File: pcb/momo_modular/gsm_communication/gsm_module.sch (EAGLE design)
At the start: 22 parts, among them U1 PIC16LF1823, U2 TI-HIGHSIDE-PFET, U3 SIM900, U4 ESD-SMF05C

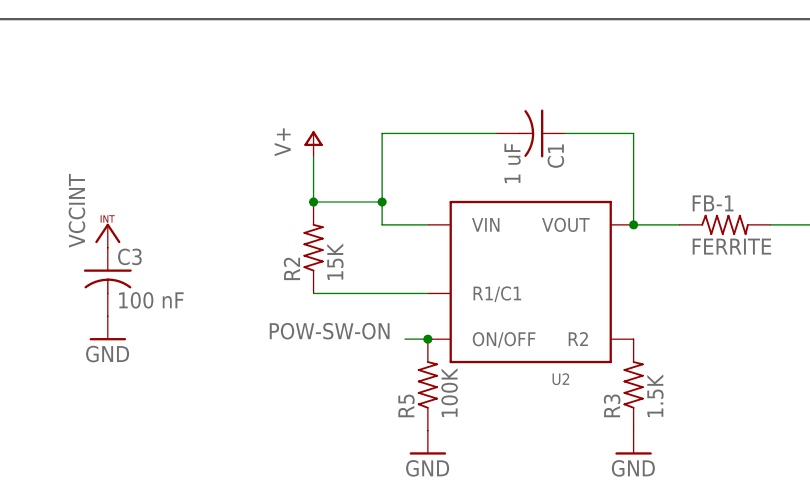
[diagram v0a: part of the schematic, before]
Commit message: Fixed C1 wiring to properly do soft-start
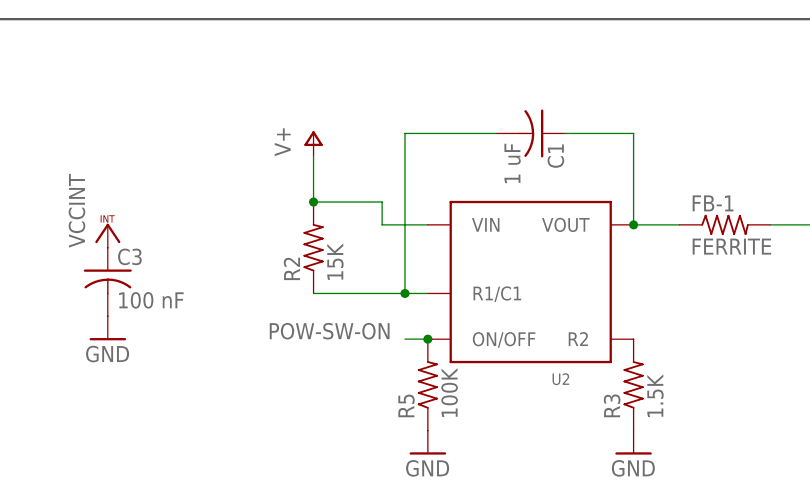
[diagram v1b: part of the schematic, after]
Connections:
- net N$3: now also C1.2
- net V+: no longer C1.2
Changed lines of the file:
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@@
 <?xml version="1.0" encoding="utf-8"?>
 <!DOCTYPE eagle SYSTEM "eagle.dtd">
-<eagle version="6.4">
+<eagle version="6.5.0">
 <drawing>
 <settings>
@@
 <wire x1="78.74" y1="93.98" x2="71.12" y2="93.98" width="0.1524" layer="91"/>
 <junction x="71.12" y="93.98"/>
-<pinref part="C1" gate="G$1" pin="2"/>
-<wire x1="91.44" y1="101.6" x2="78.74" y2="101.6" width="0.1524" layer="91"/>
-<wire x1="78.74" y1="101.6" x2="78.74" y2="93.98" width="0.1524" layer="91"/>
-<junction x="78.74" y="93.98"/>
 <pinref part="U2" gate="G$1" pin="VIN"/>
 </segment>
@@
 <segment>
 <pinref part="R2" gate="G$1" pin="1"/>
-<wire x1="71.12" y1="83.82" x2="83.82" y2="83.82" width="0.1524" layer="91"/>
+<wire x1="71.12" y1="83.82" x2="81.28" y2="83.82" width="0.1524" layer="91"/>
 <pinref part="U2" gate="G$1" pin="R1/C1"/>
-</segment>
-</net>
+<pinref part="C1" gate="G$1" pin="2"/>
+<wire x1="81.28" y1="83.82" x2="83.82" y2="83.82" width="0.1524" layer="91"/>
+<wire x1="91.44" y1="101.6" x2="81.28" y2="101.6" width="0.1524" layer="91"/>
+<wire x1="81.28" y1="101.6" x2="81.28" y2="83.82" width="0.1524" layer="91"/>
+<junction x="81.28" y="83.82"/>
+</segment>
+</net>

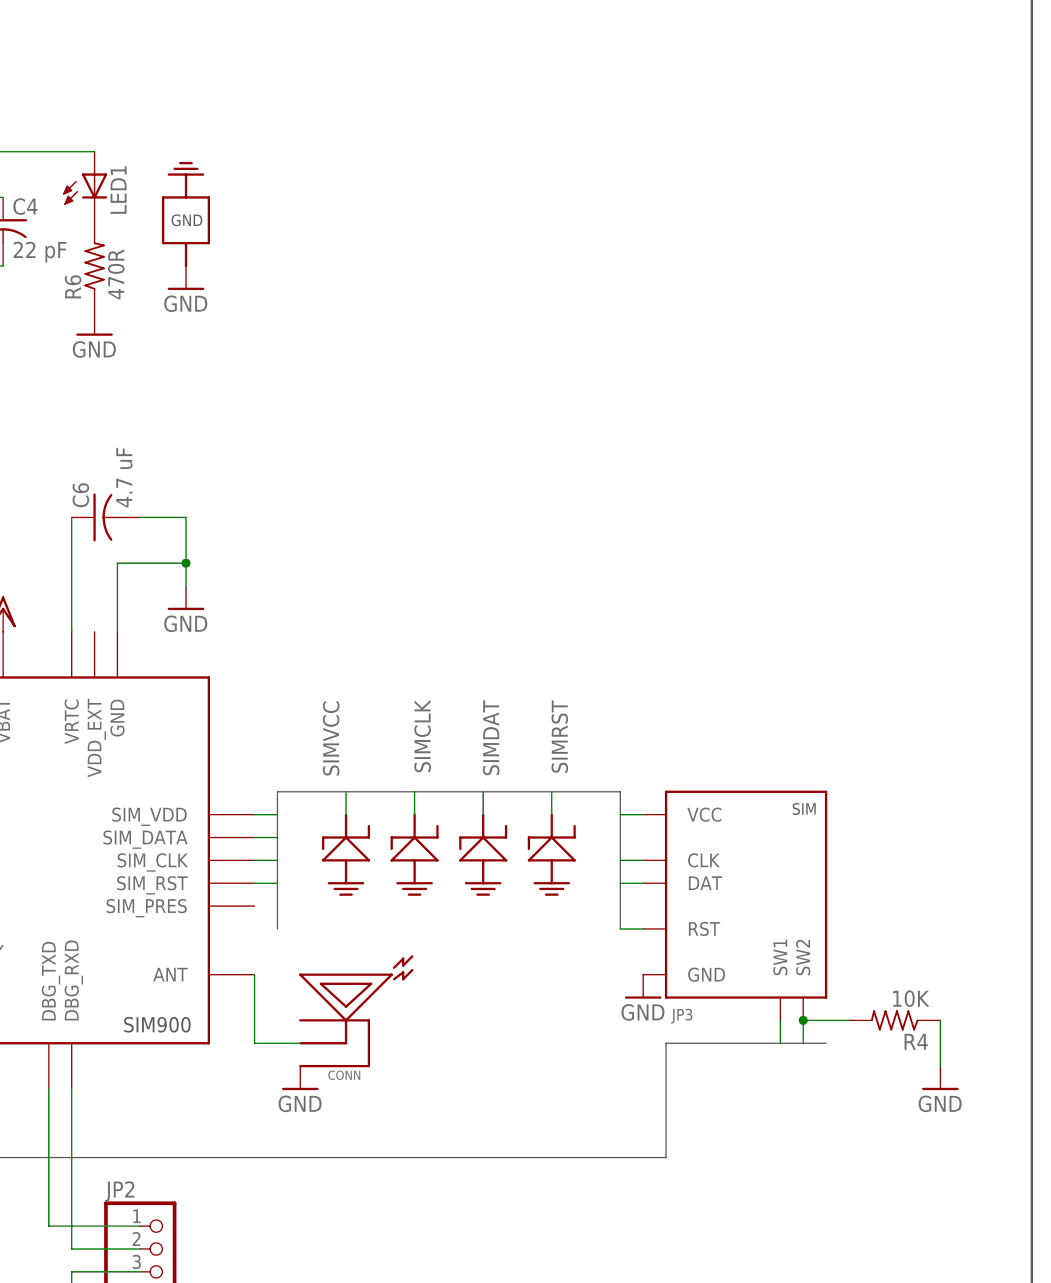
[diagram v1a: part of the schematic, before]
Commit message: Re-layout gsm_module to use sd/card adapter
Board is now 2" long, fitting a 1M form-factor and allowing the
controller board to be expanded in order to make more space for
power connectors.
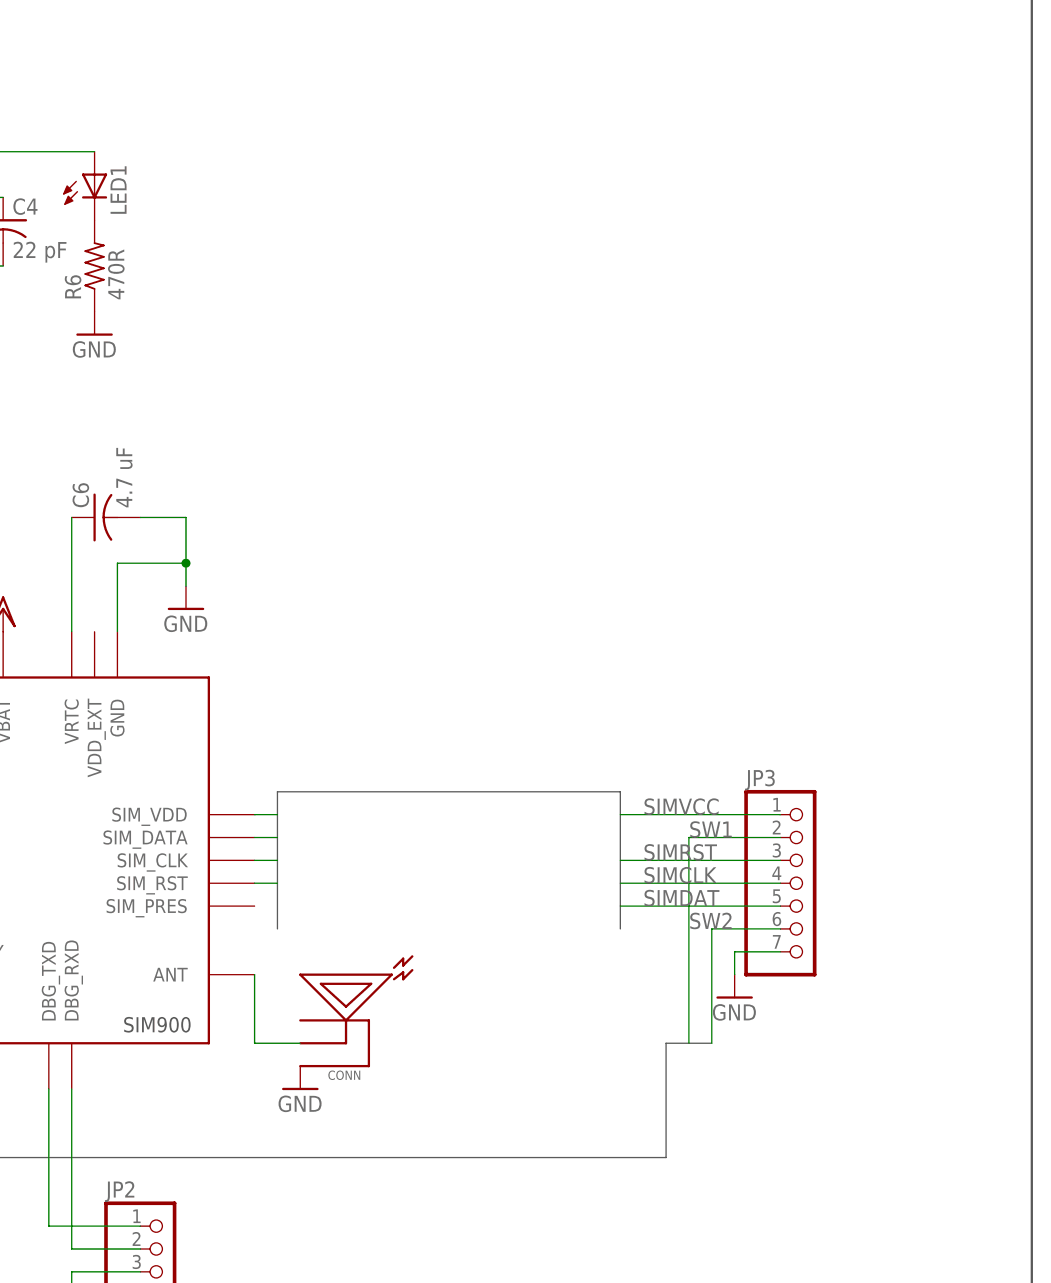
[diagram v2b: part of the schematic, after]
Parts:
- removed R4: 10K, rcl:R-US_R0603
- removed U4: ESD-SMF05C, components:ESD-SMF05C
- JP3: value SIMHOLDER-8PINHING -> (none); device components:SIMHOLDER-8PINHING -> pinhead:PINHD-1X7
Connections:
- net GND: now also JP3.7; no longer JP3.GND, R4.1, U4G$6.GND
- net SIMCLK: now also JP3.4; no longer JP3.CLK, U4G$4.P$1
- net SIMDAT: now also JP3.5; no longer JP3.DAT, U4G$3.P$1
- net SIMRST: now also JP3.3; no longer JP3.RST, U4G$2.P$1
- net SIMVCC: now also JP3.1; no longer JP3.VCC, U4G$1.P$1
- net SW1: now also JP3.2; no longer JP3.SW1
- net SW2: now also JP3.6; no longer JP3.SW2, R4.2
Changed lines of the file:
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@@
 <?xml version="1.0" encoding="utf-8"?>
 <!DOCTYPE eagle SYSTEM "eagle.dtd">
-<eagle version="6.5.0">
+<eagle version="6.4">
 <drawing>
 <settings>
@@
 <part name="VDD2" library="supply1" deviceset="VDD" device=""/>
 <part name="GND7" library="supply1" deviceset="GND" device=""/>
-<part name="GND11" library="supply1" deviceset="GND" device=""/>
-<part name="GND12" library="supply1" deviceset="GND" device=""/>
 <part name="CONN" library="components" deviceset="RFANTENNA" device="">
 <attribute name="DIGIKEY-PN" value="J983CT-ND"/>
@@
 <part name="VCC4" library="supply1" deviceset="VCCINT" device=""/>
 <part name="GND14" library="supply1" deviceset="GND" device=""/>
-<part name="U4" library="components" deviceset="ESD-SMF05C" device=""/>
 <part name="C2" library="rcl" deviceset="C-US" device="C0402K" value="47 pF">
 <attribute name="DIGIKEY-PN" value="445-1243-1-ND"/>
@@
 <part name="C4" library="rcl" deviceset="C-US" device="C0402K" value="22 pF">
 <attribute name="DIGIKEY-PN" value="445-1239-1-ND"/>
-</part>
-<part name="R4" library="rcl" deviceset="R-US_" device="R0603" value="10K">
-<attribute name="DIGIKEY-PN" value="P10.0KHCT-ND"/>
 </part>
 <part name="JP2" library="pinhead" deviceset="PINHD-1X3" device=""/>
@@
 <part name="U3" library="components" deviceset="SIM900" device=""/>
 <part name="C5" library="components" deviceset="TANTALUM_CAP" device="" value="330 uF"/>
-<part name="JP3" library="components" deviceset="SIMHOLDER-8PIN" device="HING"/>
-<part name="GND8" library="supply1" deviceset="GND" device=""/>
 <part name="GND9" library="supply1" deviceset="GND" device=""/>
 <part name="LED1" library="led" deviceset="LED" device="CHIPLED_0603">
@@
 <attribute name="DIGIKEY-PN" value="1276-1259-1-ND"/>
 </part>
+<part name="JP3" library="pinhead" deviceset="PINHD-1X7" device=""/>
+<part name="GND8" library="supply1" deviceset="GND" device=""/>
 </parts>
 <sheets>
@@
 <instance part="VDD2" gate="G$1" x="152.4" y="40.64"/>
 <instance part="GND7" gate="1" x="172.72" y="40.64"/>
-<instance part="GND11" gate="1" x="223.52" y="-2.54"/>
-<instance part="GND12" gate="1" x="172.72" y="76.2"/>
 <instance part="CONN" gate="G$1" x="185.42" y="-10.16">
 <attribute name="DIGIKEY-PN" x="185.42" y="-10.16" size="1.778" layer="96" display="off"/>
@@
 <instance part="VCC4" gate="G$1" x="48.26" y="91.44"/>
 <instance part="GND14" gate="1" x="48.26" y="78.74"/>
-<instance part="U4" gate="G$1" x="190.5" y="15.24"/>
-<instance part="U4" gate="G$4" x="198.12" y="15.24"/>
-<instance part="U4" gate="G$3" x="205.74" y="15.24"/>
-<instance part="U4" gate="G$2" x="213.36" y="15.24"/>
-<instance part="U4" gate="G$6" x="172.72" y="83.82" rot="R180"/>
 <instance part="C2" gate="G$1" x="144.78" y="83.82">
 <attribute name="DIGIKEY-PN" x="144.78" y="83.82" size="1.778" layer="96" display="off"/>
@@
 <instance part="C4" gate="G$1" x="152.4" y="83.82">
 <attribute name="DIGIKEY-PN" x="152.4" y="83.82" size="1.778" layer="96" display="off"/>
-</instance>
-<instance part="R4" gate="G$1" x="251.46" y="-5.08" rot="R180">
-<attribute name="DIGIKEY-PN" x="251.46" y="-5.08" size="1.778" layer="96" rot="R180" display="off"/>
 </instance>
 <instance part="JP2" gate="A" x="170.18" y="-30.48"/>
@@
 <instance part="U3" gate="G$1" x="152.4" y="15.24"/>
 <instance part="C5" gate="G$1" x="132.08" y="81.28"/>
-<instance part="JP3" gate="G$1" x="226.06" y="5.08"/>
-<instance part="GND8" gate="1" x="256.54" y="-12.7"/>
 <instance part="GND9" gate="1" x="144.78" y="76.2"/>
 <instance part="LED1" gate="G$1" x="162.56" y="88.9">
@@
 <attribute name="DIGIKEY-PN" x="162.56" y="50.8" size="1.778" layer="96" rot="R90" display="off"/>
 </instance>
+<instance part="JP3" gate="A" x="241.3" y="10.16"/>
+<instance part="GND8" gate="1" x="233.68" y="-2.54"/>
 </instances>
 <busses>
@@
 <wire x1="132.08" y1="-20.32" x2="226.06" y2="-20.32" width="0.762" layer="92"/>
 <wire x1="226.06" y1="-20.32" x2="226.06" y2="-7.62" width="0.762" layer="92"/>
-<wire x1="226.06" y1="-7.62" x2="243.84" y2="-7.62" width="0.762" layer="92"/>
+<wire x1="226.06" y1="-7.62" x2="231.14" y2="-7.62" width="0.762" layer="92"/>
 </segment>
 </bus>
@@
 </segment>
 <segment>
-<pinref part="GND12" gate="1" pin="GND"/>
-<pinref part="U4" gate="G$6" pin="GND"/>
-</segment>
-<segment>
 <pinref part="GND6" gate="1" pin="GND"/>
 <wire x1="160.02" y1="-38.1" x2="160.02" y2="-33.02" width="0.1524" layer="91"/>
@@
 <pinref part="GND5" gate="1" pin="GND"/>
 <pinref part="C5" gate="G$1" pin="-"/>
-</segment>
-<segment>
-<pinref part="GND11" gate="1" pin="GND"/>
-<pinref part="JP3" gate="G$1" pin="GND"/>
-</segment>
-<segment>
-<pinref part="R4" gate="G$1" pin="1"/>
-<pinref part="GND8" gate="1" pin="GND"/>
-<wire x1="256.54" y1="-5.08" x2="256.54" y2="-10.16" width="0.1524" layer="91"/>
 </segment>
 <segment>
@@
 <pinref part="GND10" gate="1" pin="GND"/>
 <pinref part="R6" gate="G$1" pin="1"/>
+</segment>
+<segment>
+<pinref part="GND8" gate="1" pin="GND"/>
+<wire x1="233.68" y1="0" x2="233.68" y2="2.54" width="0.1524" layer="91"/>
+<pinref part="JP3" gate="A" pin="7"/>
+<wire x1="233.68" y1="2.54" x2="238.76" y2="2.54" width="0.1524" layer="91"/>
 </segment>
 </net>
@@
 </segment>
 <segment>
-<wire x1="220.98" y1="17.78" x2="223.52" y2="17.78" width="0.1524" layer="91"/>
-<pinref part="JP3" gate="G$1" pin="VCC"/>
-</segment>
-<segment>
-<wire x1="190.5" y1="17.78" x2="190.5" y2="20.32" width="0.1524" layer="91"/>
-<pinref part="U4" gate="G$1" pin="P$1"/>
-<label x="187.96" y="30.48" size="1.778" layer="95" rot="R270"/>
+<pinref part="JP3" gate="A" pin="1"/>
+<wire x1="220.98" y1="17.78" x2="238.76" y2="17.78" width="0.1524" layer="91"/>
+<label x="223.52" y="17.78" size="1.778" layer="95"/>
 </segment>
 </net>
@@
 </segment>
 <segment>
-<wire x1="220.98" y1="10.16" x2="223.52" y2="10.16" width="0.1524" layer="91"/>
-<pinref part="JP3" gate="G$1" pin="DAT"/>
-</segment>
-<segment>
-<wire x1="205.74" y1="17.78" x2="205.74" y2="20.32" width="0.1524" layer="91"/>
-<pinref part="U4" gate="G$3" pin="P$1"/>
-<label x="205.74" y="30.48" size="1.778" layer="95" rot="R270"/>
+<pinref part="JP3" gate="A" pin="5"/>
+<wire x1="220.98" y1="7.62" x2="238.76" y2="7.62" width="0.1524" layer="91"/>
+<label x="223.52" y="7.62" size="1.778" layer="95"/>
 </segment>
 </net>
@@
 </segment>
 <segment>
-<wire x1="220.98" y1="12.7" x2="223.52" y2="12.7" width="0.1524" layer="91"/>
-<pinref part="JP3" gate="G$1" pin="CLK"/>
-</segment>
-<segment>
-<wire x1="198.12" y1="17.78" x2="198.12" y2="20.32" width="0.1524" layer="91"/>
-<pinref part="U4" gate="G$4" pin="P$1"/>
-<label x="198.12" y="30.48" size="1.778" layer="95" rot="R270"/>
+<pinref part="JP3" gate="A" pin="4"/>
+<wire x1="220.98" y1="10.16" x2="238.76" y2="10.16" width="0.1524" layer="91"/>
+<label x="223.52" y="10.16" size="1.778" layer="95"/>
 </segment>
 </net>
@@
 </segment>
 <segment>
-<wire x1="220.98" y1="5.08" x2="223.52" y2="5.08" width="0.1524" layer="91"/>
-<pinref part="JP3" gate="G$1" pin="RST"/>
-</segment>
-<segment>
-<wire x1="213.36" y1="17.78" x2="213.36" y2="20.32" width="0.1524" layer="91"/>
-<pinref part="U4" gate="G$2" pin="P$1"/>
-<label x="213.36" y="30.48" size="1.778" layer="95" rot="R270"/>
+<pinref part="JP3" gate="A" pin="3"/>
+<wire x1="220.98" y1="12.7" x2="238.76" y2="12.7" width="0.1524" layer="91"/>
+<label x="223.52" y="12.7" size="1.778" layer="95"/>
 </segment>
 </net>
@@
 </segment>
 <segment>
-<pinref part="JP3" gate="G$1" pin="SW1"/>
-<wire x1="238.76" y1="-5.08" x2="238.76" y2="-7.62" width="0.1524" layer="91"/>
+<wire x1="228.6" y1="-7.62" x2="228.6" y2="15.24" width="0.1524" layer="91"/>
+<pinref part="JP3" gate="A" pin="2"/>
+<wire x1="228.6" y1="15.24" x2="238.76" y2="15.24" width="0.1524" layer="91"/>
+<label x="228.6" y="15.24" size="1.778" layer="95"/>
 </segment>
 </net>
 <net name="SW2" class="0">
-<segment>
-<pinref part="JP3" gate="G$1" pin="SW2"/>
-<wire x1="241.3" y1="-5.08" x2="241.3" y2="-7.62" width="0.1524" layer="91"/>
-<pinref part="R4" gate="G$1" pin="2"/>
-<wire x1="246.38" y1="-5.08" x2="241.3" y2="-5.08" width="0.1524" layer="91"/>
-<junction x="241.3" y="-5.08"/>
-</segment>
 <segment>
 <pinref part="U1" gate="G$1" pin="RA0"/>
@@
 <label x="33.02" y="20.32" size="1.778" layer="95"/>
 </segment>
-</net>
+<segment>
+<wire x1="231.14" y1="-7.62" x2="231.14" y2="5.08" width="0.1524" layer="91"/>
+<pinref part="JP3" gate="A" pin="6"/>
+<wire x1="231.14" y1="5.08" x2="238.76" y2="5.08" width="0.1524" layer="91"/>
+<label x="228.6" y="5.08" size="1.778" layer="95"/>
+</segment>
+</net>
